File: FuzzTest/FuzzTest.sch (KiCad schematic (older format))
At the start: 15 parts, among them Q1 BC108, Q2 BC108

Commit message: Getting a decent square wave now
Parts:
- removed C2: 20u, symbol pspice:C
- removed R5: 100k, symbol pspice:R
- added C2: 20u, symbol Device:CP
- GAIN: value 100 -> 1k
- LOAD: value 300 -> 50k
- R3: value 330 -> 470
- V1: value dc 0 ac sin(0 100m 500) -> dc 0 ac sin(0 20m 1k)
- VOL: value 500k -> 300k
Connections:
- net 0: now also C2.2
- net at GAIN.2: now also C2.1
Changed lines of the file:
@@
 EESchema Schematic File Version 4
+LIBS:FuzzTest-cache
 EELAYER 26 0
 EELAYER END
@@
 	8300 1150 7850 1150
 Connection ~ 7850 1150
-Wire Wire Line
-	8600 1250 8450 1250
-Wire Wire Line
-	8450 1250 8450 1100
 $Comp
 L Device:R R2
@@
 P 8600 2050
 F 0 "GAIN" H 8530 2096 50  0000 R CNN
-F 1 "100" H 8530 2005 50  0000 R CNN
+F 1 "1k" H 8530 2005 50  0000 R CNN
 F 2 "" H 8600 2050 50  0001 C CNN
 F 3 "~" H 8600 2050 50  0001 C CNN
@@
 out
 $Comp
-L pspice:0 #GND?
+L pspice:0 #GND0101
 U 1 1 5C5E0272
 P 8600 2300
-F 0 "#GND?" H 8600 2200 50  0001 C CNN
+F 0 "#GND0101" H 8600 2200 50  0001 C CNN
 F 1 "0" H 8600 2387 50  0000 C CNN
 F 2 "" H 8600 2300 50  0001 C CNN
@@
 $EndComp
 $Comp
-L pspice:0 #GND?
+L pspice:0 #GND0102
 U 1 1 5C5E02B2
 P 8900 2850
-F 0 "#GND?" H 8900 2750 50  0001 C CNN
+F 0 "#GND0102" H 8900 2750 50  0001 C CNN
 F 1 "0" H 8900 2937 50  0000 C CNN
 F 2 "" H 8900 2850 50  0001 C CNN
@@
 $EndComp
 $Comp
-L pspice:0 #GND?
+L pspice:0 #GND0103
 U 1 1 5C5E02F2
 P 6700 2950
-F 0 "#GND?" H 6700 2850 50  0001 C CNN
+F 0 "#GND0103" H 6700 2850 50  0001 C CNN
 F 1 "0" H 6700 3037 50  0000 C CNN
 F 2 "" H 6700 2950 50  0001 C CNN
@@
 $EndComp
 $Comp
-L pspice:0 #GND?
+L pspice:0 #GND0104
 U 1 1 5C5E0332
 P 6150 2250
-F 0 "#GND?" H 6150 2150 50  0001 C CNN
+F 0 "#GND0104" H 6150 2150 50  0001 C CNN
 F 1 "0" H 6150 2337 50  0000 C CNN
 F 2 "" H 6150 2250 50  0001 C CNN
@@
 P 6150 1800
 F 0 "V1" H 6378 1846 50  0000 L CNN
-F 1 "dc 0 ac sin(0 100m 500)" H 6378 1755 50  0000 L CNN
+F 1 "dc 0 ac sin(0 20m 1k)" H 6378 1755 50  0000 L CNN
 F 2 "" H 6150 1800 50  0001 C CNN
 F 3 "~" H 6150 1800 50  0001 C CNN
@@
 P 9050 950
 F 0 "VOL" H 8980 996 50  0000 R CNN
-F 1 "500k" H 8980 905 50  0000 R CNN
+F 1 "300k" H 8980 905 50  0000 R CNN
 F 2 "" H 9050 950 50  0001 C CNN
 F 3 "~" H 9050 950 50  0001 C CNN
@@
 $EndComp
 $Comp
-L pspice:0 #GND?
+L pspice:0 #GND0105
 U 1 1 5C5E102A
 P 9050 1250
-F 0 "#GND?" H 9050 1150 50  0001 C CNN
+F 0 "#GND0105" H 9050 1150 50  0001 C CNN
 F 1 "0" H 9050 1337 50  0000 C CNN
 F 2 "" H 9050 1250 50  0001 C CNN
@@
 P 9250 1200
 F 0 "LOAD" H 9320 1246 50  0000 L CNN
-F 1 "300" H 9320 1155 50  0000 L CNN
+F 1 "50k" H 9320 1155 50  0000 L CNN
 F 2 "" V 9180 1200 50  0001 C CNN
 F 3 "~" H 9250 1200 50  0001 C CNN
@@
 $EndComp
 $Comp
-L pspice:0 #GND?
+L pspice:0 #GND0106
 U 1 1 5C5E28AF
 P 9250 1500
-F 0 "#GND?" H 9250 1400 50  0001 C CNN
+F 0 "#GND0106" H 9250 1400 50  0001 C CNN
 F 1 "0" H 9250 1587 50  0000 C CNN
 F 2 "" H 9250 1500 50  0001 C CNN
@@
 Wire Wire Line
 	9250 950  9300 950
-$Comp
-L pspice:C C2
-U 1 1 5C5E4A06
-P 8900 2300
-F 0 "C2" H 9078 2346 50  0000 L CNN
-F 1 "20u" H 9078 2255 50  0000 L CNN
-F 2 "" H 8900 2300 50  0001 C CNN
-F 3 "~" H 8900 2300 50  0001 C CNN
-F 4 "C" H 8900 2300 50  0001 C CNN "Spice_Primitive"
-F 5 "20u" H 8900 2300 50  0001 C CNN "Spice_Model"
-F 6 "Y" H 8900 2300 50  0001 C CNN "Spice_Netlist_Enabled"
-	1    8900 2300
-	1    0    0    -1
-$EndComp
-Wire Wire Line
-	8900 2550 8900 2850
 $Comp
 L pspice:C C1
@@
 	6700 2800 6700 2950
 Wire Wire Line
-	7450 1350 7550 1350
-Wire Wire Line
 	6950 1350 6700 1350
 $Comp
@@
 P 8100 800
 F 0 "R3" V 7895 800 50  0000 C CNN
-F 1 "330" V 7986 800 50  0000 C CNN
+F 1 "470" V 7986 800 50  0000 C CNN
 F 2 "" H 8100 800 50  0001 C CNN
 F 3 "~" H 8100 800 50  0001 C CNN
@@
 	7850 800  7850 750
 $Comp
-L pspice:R R5
-U 1 1 5C5E837C
-P 7450 1650
-F 0 "R5" H 7518 1696 50  0000 L CNN
-F 1 "100k" H 7518 1605 50  0000 L CNN
-F 2 "" H 7450 1650 50  0001 C CNN
-F 3 "~" H 7450 1650 50  0001 C CNN
-	1    7450 1650
-	1    0    0    -1
-$EndComp
-Wire Wire Line
-	7450 1400 7450 1350
-Connection ~ 7450 1350
-$Comp
-L pspice:0 #GND?
+L pspice:0 #GND0107
 U 1 1 5C5E89B5
 P 7450 2050
-F 0 "#GND?" H 7450 1950 50  0001 C CNN
+F 0 "#GND0107" H 7450 1950 50  0001 C CNN
 F 1 "0" H 7450 2137 50  0000 C CNN
 F 2 "" H 7450 2050 50  0001 C CNN
@@
 	7450 2050 7450 1900
 Wire Wire Line
+	7600 1800 8050 1800
+Wire Wire Line
+	7450 1900 7850 1900
+Wire Wire Line
+	7850 1900 7850 1550
+Wire Wire Line
+	7450 1350 7550 1350
+Wire Wire Line
 	7600 1800 7600 1350
 Wire Wire Line
 	7600 1350 7550 1350
-Wire Wire Line
-	7600 1800 8050 1800
 Connection ~ 7550 1350
-Wire Wire Line
-	7450 1900 7850 1900
-Wire Wire Line
-	7850 1900 7850 1550
-Connection ~ 7450 1900
+$Comp
+L Device:CP C2
+U 1 1 5C64591E
+P 8900 2200
+F 0 "C2" H 9018 2246 50  0000 L CNN
+F 1 "20u" H 9018 2155 50  0000 L CNN
+F 2 "" H 8938 2050 50  0001 C CNN
+F 3 "~" H 8900 2200 50  0001 C CNN
+	1    8900 2200
+	1    0    0    -1
+$EndComp
+Wire Wire Line
+	8900 2350 8900 2850
+Wire Wire Line
+	8600 1250 8450 1250
+Wire Wire Line
+	8450 1250 8450 1100
 $EndSCHEMATC

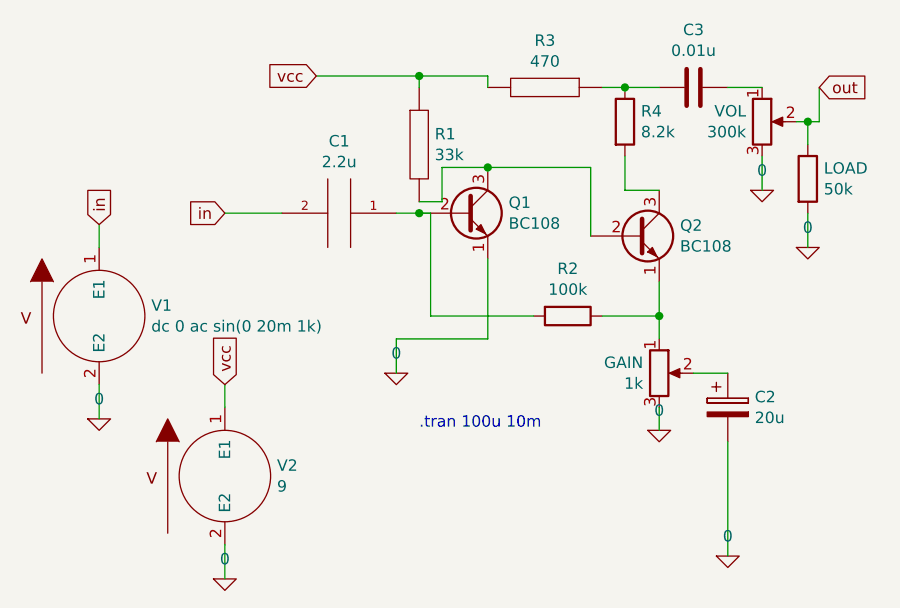
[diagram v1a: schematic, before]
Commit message: Create rats nest for pcb layout
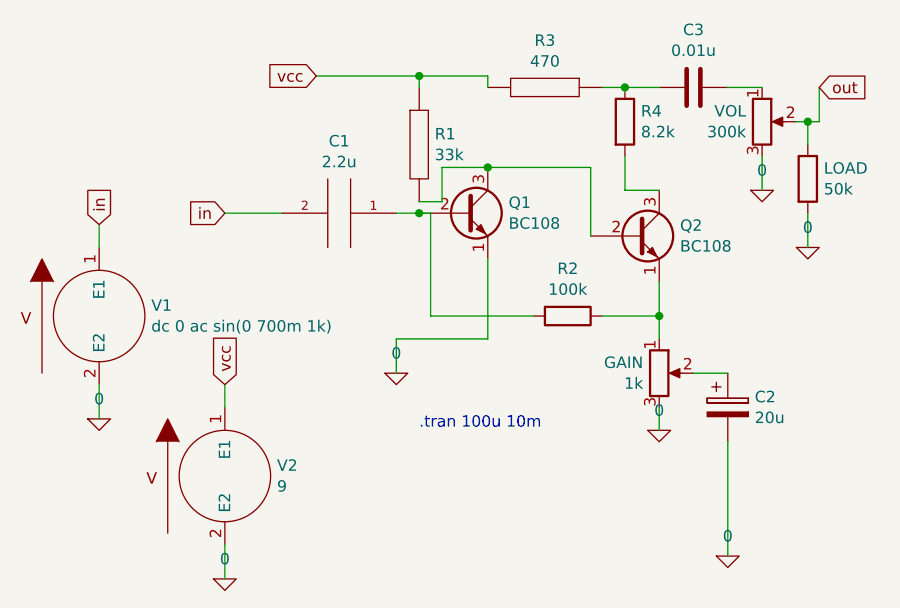
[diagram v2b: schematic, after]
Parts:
- V1: value dc 0 ac sin(0 20m 1k) -> dc 0 ac sin(0 700m 1k)
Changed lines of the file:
@@
 P 6150 1800
 F 0 "V1" H 6378 1846 50  0000 L CNN
-F 1 "dc 0 ac sin(0 20m 1k)" H 6378 1755 50  0000 L CNN
+F 1 "dc 0 ac sin(0 700m 1k)" H 6378 1755 50  0000 L CNN
 F 2 "" H 6150 1800 50  0001 C CNN
 F 3 "~" H 6150 1800 50  0001 C CNN
